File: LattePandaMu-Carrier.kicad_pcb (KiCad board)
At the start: 4 copper layers, 165 x 100 mm, 218 parts, among them J1 Conn_01x03_Pin, J10 Conn_01x03_Pin, J11 Conn_01x03_Pin, J12 Conn_01x04_Pin, J13 Conn_01x04_Pin, J14 Conn_01x03_Pin, J15 Bus_M.2_Socket_M, J16 Bus_M.2_Socket_E, J17 Barrel_Jack_Switch, J18 USB_C_Receptacle_USB2.0_16P, J19 Conn_01x04_Pin, J20 Conn_01x04_Pin, J21 Conn_01x04_Pin, J3 HDMI_A, J4 USB3_A_Stacked, J5 USB_A_Stacked, J6 RJ45_RB1-125B8G1A, J7 Conn_01x04_Pin, J8 Conn_01x03_Pin, J9 Conn_01x04_Pin, M1 Fan_4pin, Q1 2SK3018, Q2 2SK3018, Q3 2SK3018, Q4 2SK3018, Q8 2N7002, SW1 SW_Push, SW2 SW_Push, U1 D3V3XA4B10LP, U10 ULC0524P, U11 ULC0524P, U12 ULC0524P, U14 USB PD等快充协议受电芯片-CH224K-ESSOP10, U15 LM2734X, U16 LM2734X, U17 ULC0524P, U2 D3V3XA4B10LP, U3 D3V3XA4B10LP, U4 D3V3XA4B10LP, U5 D3V3XA4B10LP, U6 RTL8111H-CG-RH, U7 ULC0524P, U8 ULC0524P, U9 ULC0524P, Y1 25MHz

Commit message: feat(routing): GPIO routing
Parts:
- moved U17 300.2 mm to (111.8, 72.2)
- moved U11 295.5 mm to (111.7, 69.0)
- moved U9 291.4 mm to (111.7, 63.6)
- moved U12 230.4 mm to (184.9, 64.9), turned to 180 degrees
- moved U10 223.4 mm to (184.9, 69.0), turned to 180 degrees
- moved R2 187.6 mm to (147.8, 126.8), turned to -90 degrees
- moved TP78 186.3 mm to (151.0, 127.2)
- moved R77 171.2 mm to (163.5, 125.5), turned to -90 degrees
- moved R76 170.6 mm to (164.5, 125.5), turned to -90 degrees
- moved J11 148.9 mm to (202.5, 65.7), turned to 180 degrees
- moved J14 142.6 mm to (198.8, 65.7), turned to 180 degrees
- moved J8 134.9 mm to (193.9, 65.7), turned to 180 degrees
- moved J10 128.9 mm to (190.2, 65.7), turned to 180 degrees
- moved J1 21.9 mm to (95.7, 60.2), turned to 0 degrees
- moved J19 5.56 mm to (99.8, 60.2)
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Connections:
- U10 pad 2: /GPIO/SOC_UART1_RX -> /GPIO/SOC_UART0_TX
- U10 pad 4: /GPIO/SOC_UART2_RX -> /GPIO/SOC_UART1_RX
- U10 pad 5: Net-(U10-NC-Pad6) -> /GPIO/SOC_UART1_TX
- U10 pad 6: Net-(U10-NC-Pad6) -> /GPIO/SOC_UART1_TX
- U10 pad 7: /GPIO/SOC_UART2_RX -> /GPIO/SOC_UART1_RX
- U10 pad 9: /GPIO/SOC_UART1_RX -> /GPIO/SOC_UART0_TX
- U11 pad 1: /GPIO/I2C2_SCL -> /GPIO/I2C4_SDA
- U11 pad 10: /GPIO/I2C2_SCL -> /GPIO/I2C4_SDA
- U11 pad 2: /GPIO/I2C3_SCL -> /GPIO/I2C4_SCL
- U11 pad 4: /GPIO/I2C4_SCL -> /GPIO/I2C5_SDA
- U11 pad 7: /GPIO/I2C4_SCL -> /GPIO/I2C5_SDA
- U11 pad 9: /GPIO/I2C3_SCL -> /GPIO/I2C4_SCL
- U12 pad 1: /GPIO/SOC_UART0_TX -> /GPIO/SOC_UART2_RX
- U12 pad 10: /GPIO/SOC_UART0_TX -> /GPIO/SOC_UART2_RX
- U12 pad 2: /GPIO/SOC_UART1_TX -> /GPIO/SOC_UART2_TX
- U12 pad 4: /GPIO/SOC_UART2_TX -> Net-(U12-NC-Pad7)
- U12 pad 7: /GPIO/SOC_UART2_TX -> Net-(U12-NC-Pad7)
- U12 pad 9: /GPIO/SOC_UART1_TX -> /GPIO/SOC_UART2_TX
- U9 pad 2: /GPIO/I2C3_SDA -> /GPIO/I2C2_SCL
- U9 pad 4: /GPIO/I2C4_SDA -> /GPIO/I2C3_SDA
- U9 pad 5: /GPIO/I2C5_SDA -> /GPIO/I2C3_SCL
- U9 pad 6: /GPIO/I2C5_SDA -> /GPIO/I2C3_SCL
- U9 pad 7: /GPIO/I2C4_SDA -> /GPIO/I2C3_SDA
- U9 pad 9: /GPIO/I2C3_SDA -> /GPIO/I2C2_SCL
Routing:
- net /GPIO/I2C2_SCL: track 0.00 -> 102.5 mm, vias 0 -> 2
- net /GPIO/I2C2_SDA: track 0.00 -> 99.8 mm, vias 0 -> 2
- net /GPIO/I2C3_SCL: track 0.00 -> 99.6 mm, vias 0 -> 2
- net /GPIO/GPP_D0: track 0.00 -> 98.7 mm, vias 0 -> 2
- net /GPIO/SOC_UART1_RX: track 0.00 -> 98.2 mm, vias 0 -> 2
- net /GPIO/SOC_UART0_RX: track 0.00 -> 98.0 mm, vias 0 -> 2
- net /GPIO/SOC_UART2_RX: track 0.00 -> 97.3 mm, vias 0 -> 2
- net /GPIO/GPP_D1: track 0.00 -> 96.7 mm, vias 0 -> 2
- net /GPIO/GPP_D2: track 0.00 -> 96.6 mm, vias 0 -> 2
- net /GPIO/I2C4_SCL: track 0.00 -> 96.3 mm, vias 0 -> 2
- net /GPIO/I2C3_SDA: track 0.00 -> 96.3 mm, vias 0 -> 2
- net /GPIO/SOC_UART2_TX: track 0.00 -> 95.1 mm, vias 0 -> 2
- net /GPIO/SOC_UART1_TX: track 0.00 -> 94.9 mm, vias 0 -> 2
- net /GPIO/SOC_UART0_TX: track 0.00 -> 94.1 mm, vias 0 -> 2
- net /GPIO/I2C4_SDA: track 0.00 -> 94.1 mm, vias 0 -> 2
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
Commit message: feat(gnd): L2 and L3 GND copper fills and gnd connections.
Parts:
- moved C84 97.9 mm to (294.7, 121.9)
- moved D26 97.9 mm to (291.1, 122.4)
- moved FID78 97.9 mm to (297.9, 74.3)
- moved FID79 97.9 mm to (297.9, 76.9)
- moved R68 97.9 mm to (302.4, 118.8)
- moved R69 97.9 mm to (305.3, 108.9)
- moved R72 97.9 mm to (305.3, 114.8)
- moved TP11 97.9 mm to (302.7, 121.6)
- moved TP12 97.9 mm to (302.7, 125.1)
- moved Q8 67.0 mm to (265.5, 121.2)
- moved C64 67.0 mm to (253.0, 96.2)
- moved C65 67.0 mm to (253.0, 98.7)
- moved C67 67.0 mm to (253.0, 101.2)
- moved C68 67.0 mm to (253.0, 103.8)
- moved C70 67.0 mm to (253.0, 106.3)
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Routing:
- net GND: track 2.00 -> 266.0 mm, vias 0 -> 221
- net +5V: track 7.34 -> 11.3 mm
- net Net-(U6-CKXTAL1): track 23.7 -> 24.2 mm
- added copper zone on F.Cu, net GND
- added copper zone on In1.Cu, net GND
- added copper zone on In2.Cu, net GND

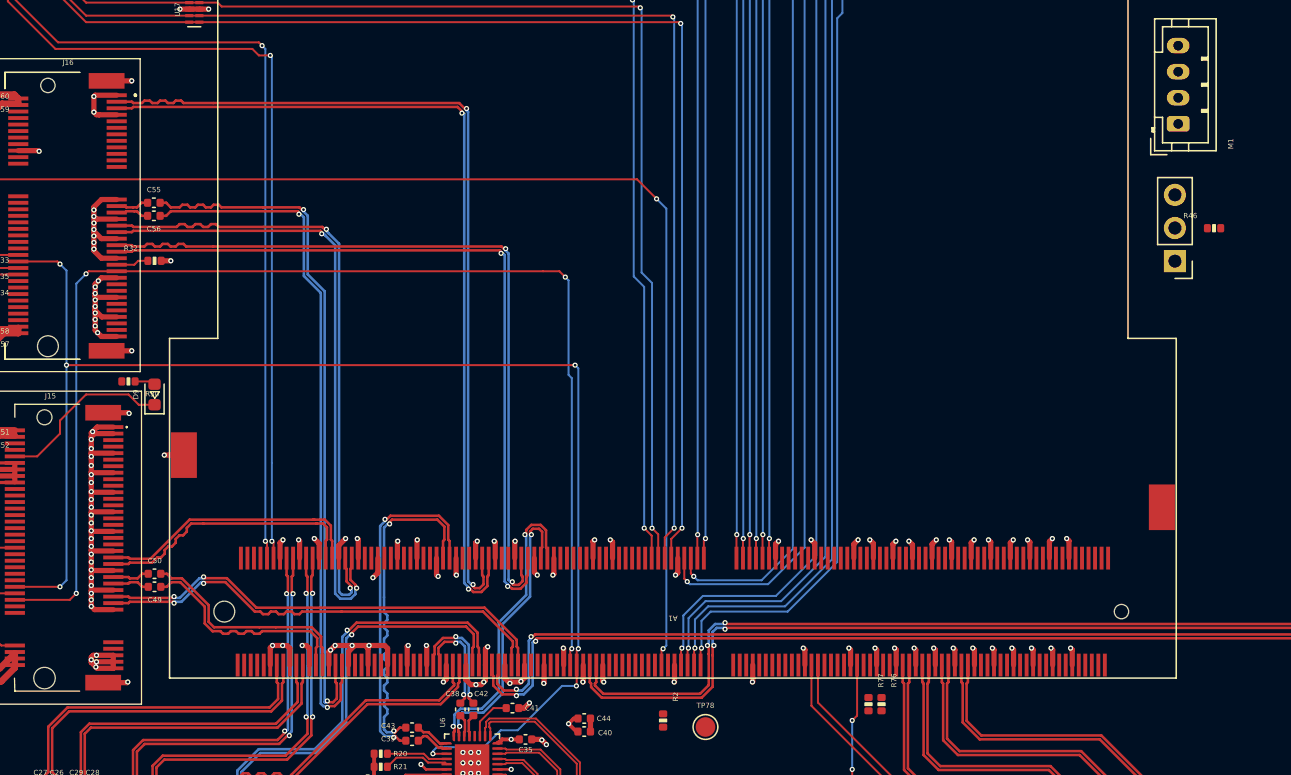
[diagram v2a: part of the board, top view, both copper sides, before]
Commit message: refactor: Reworked some gnd connections to copper fills.
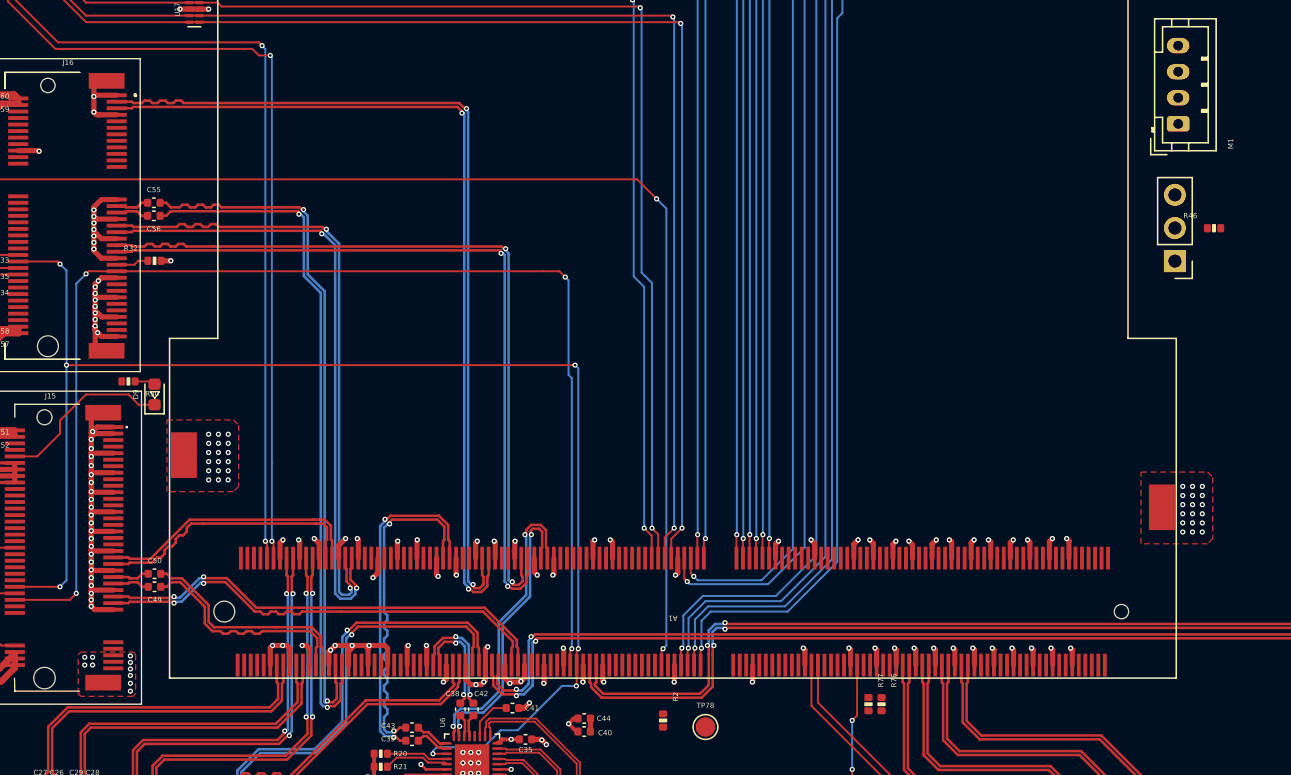
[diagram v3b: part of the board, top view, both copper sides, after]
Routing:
- net GND: track 266.0 -> 257.0 mm, vias 221 -> 258

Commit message: feat(routing): Wired cpu fan connectors and components.
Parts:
- moved SW1 155.1 mm to (74.3, 135.3), turned to 0 degrees
- moved SW2 153.9 mm to (74.3, 142.8), turned to 0 degrees
- moved BT1 142.4 mm to (218.7, 126.8), turned to 180 degrees
- moved TP11 126.1 mm to (186.5, 72.6), turned to -90 degrees
- moved TP12 124.3 mm to (190.1, 72.5), turned to -90 degrees
- moved R69 122.7 mm to (186.8, 77.1)
- moved R72 122.6 mm to (186.8, 83.2), turned to 180 degrees
- moved R68 122.2 mm to (186.8, 79.2)
- moved C84 113.3 mm to (187.8, 84.4)
- moved D26 112.5 mm to (186.3, 81.7), turned to 180 degrees
- moved U14 48.5 mm to (250.4, 90.4)
- moved R1 44.9 mm to (283.2, 114.1)
- moved R78 44.9 mm to (283.2, 122.1)
- moved R79 44.9 mm to (283.2, 124.1)
- moved D15 43.4 mm to (211.6, 72.2)
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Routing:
- net /Fan/FAN_1_TAC: track 0.00 -> 114.5 mm, vias 0 -> 2
- net /Fan/FAN_1_PWM: track 0.00 -> 114.5 mm, vias 0 -> 4
- net +5V: track 11.3 -> 24.8 mm
- net Net-(D26-A): track 0.00 -> 10.6 mm
- net GND: track 257.0 -> 261.5 mm, vias 258 -> 259
- net Net-(M1-PWM): track 0.00 -> 4.08 mm
